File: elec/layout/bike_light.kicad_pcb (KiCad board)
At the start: 2 copper layers, 40 x 40 mm, 21 parts

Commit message: update the footprint and layout
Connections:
- net 35 renamed 32
- net 37 renamed 34
- net 42 renamed 39
- net 43 renamed 40
- net 8 renamed 7
- C2 pad 1: 14 -> 11
- C3 pad 1: 19 -> 16
- D1 pad 1: 14 -> 11
- D1 pad 2: 23 -> 20
- D2 pad 1: 15 -> 12
- D2 pad 2: 20 -> 17
- D3 pad 2: 6 -> 2
- D4 pad 2: 9 -> 2
- D5 pad 1: 11 -> 9
- D5 pad 2: 12 -> 2
- J1 pad A6: 41 -> 38
- J1 pad A8: 44 -> 41
- J1 pad B6: 41 -> 38
- J1 pad B8: 44 -> 41
- J2 pad 2: 15 -> 12
- L1 pad 2: 23 -> 20
- R1 pad 1: 18 -> 15
- R2 pad 1: 14 -> 11
- R4 pad 1: 15 -> 12
- R5 pad 1: 14 -> 11
- R5 pad 2: 21 -> 18
- R6 pad 1: 21 -> 18
- U1 pad 1: 15 -> 12
- U1 pad 2: 11 -> 9
- U1 pad 4: 11 -> 9
- U2 pad 1: 15 -> 12
- U2 pad 3: 20 -> 17
- U3 pad 10: 22 -> 19
- U3 pad 13: 14 -> 11
- U3 pad 18: 23 -> 20
- U3 pad 4: 18 -> 15
- U3 pad 6: 19 -> 16
- U3 pad 7: 20 -> 17
- U3 pad 8: 21 -> 18
- U3 pad 9: 22 -> 19
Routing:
- net 12: track 0.00 -> 62.4 mm, vias 0 -> 2
- net 15: track 62.4 -> 3.92 mm, vias 2 -> 0
- net 14: track 29.5 -> 0.00 mm, vias 2 -> 0
- net 9: track 0.00 -> 18.6 mm
- net 21: track 14.6 -> 0.00 mm, vias 2 -> 0
- net 17: track 0.00 -> 14.0 mm
- net 11: track 18.6 -> 29.5 mm, vias 0 -> 2
- net 18: track 3.92 -> 14.6 mm, vias 0 -> 2
- net 20: track 14.0 -> 5.93 mm
- net 23: track 5.93 -> 0.00 mm
- net 16: track 0.00 -> 2.25 mm
- net 19: track 2.25 -> 0.50 mm
- net 22: track 0.50 -> 0.00 mm

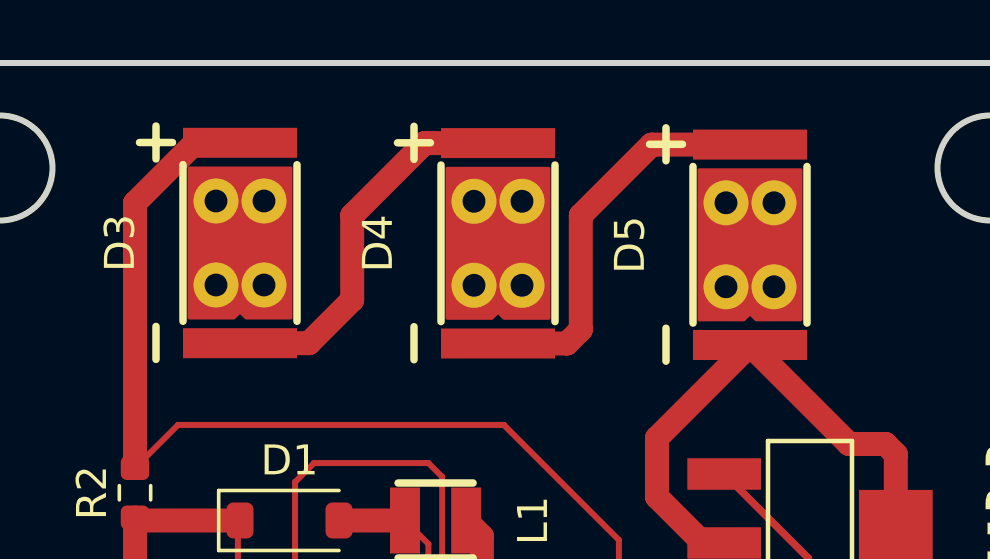
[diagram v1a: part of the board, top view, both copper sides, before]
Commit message: update footprint with thermal pad
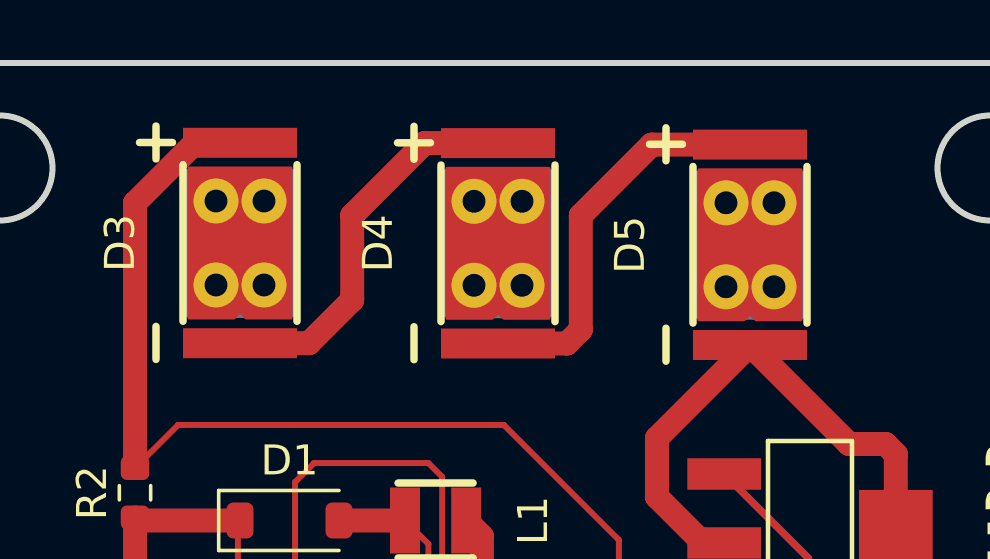
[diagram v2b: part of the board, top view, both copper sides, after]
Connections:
- net 32 renamed 35
- net 34 renamed 37
- net 39 renamed 42
- net 40 renamed 43
- net 7 renamed 8
- C2 pad 1: 11 -> 14
- C3 pad 1: 16 -> 19
- D1 pad 1: 11 -> 14
- D1 pad 2: 20 -> 23
- D2 pad 1: 12 -> 15
- D2 pad 2: 17 -> 20
- D3 pad 2: 2 -> 6
- D4 pad 2: 2 -> 9
- D5 pad 1: 9 -> 11
- D5 pad 2: 2 -> 12
- J1 pad A6: 38 -> 41
- J1 pad A8: 41 -> 44
- J1 pad B6: 38 -> 41
- J1 pad B8: 41 -> 44
- J2 pad 2: 12 -> 15
- L1 pad 2: 20 -> 23
- R1 pad 1: 15 -> 18
- R2 pad 1: 11 -> 14
- R4 pad 1: 12 -> 15
- R5 pad 1: 11 -> 14
- R5 pad 2: 18 -> 21
- R6 pad 1: 18 -> 21
- U1 pad 1: 12 -> 15
- U1 pad 2: 9 -> 11
- U1 pad 4: 9 -> 11
- U2 pad 1: 12 -> 15
- U2 pad 3: 17 -> 20
- U3 pad 10: 19 -> 22
- U3 pad 13: 11 -> 14
- U3 pad 18: 20 -> 23
- U3 pad 4: 15 -> 18
- U3 pad 6: 16 -> 19
- U3 pad 7: 17 -> 20
- U3 pad 8: 18 -> 21
- U3 pad 9: 19 -> 22
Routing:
- net 12: track 62.4 -> 0.00 mm, vias 2 -> 0
- net 15: track 3.92 -> 62.4 mm, vias 0 -> 2
- net 14: track 0.00 -> 29.5 mm, vias 0 -> 2
- net 9: track 18.6 -> 0.00 mm
- net 21: track 0.00 -> 14.6 mm, vias 0 -> 2
- net 17: track 14.0 -> 0.00 mm
- net 11: track 29.5 -> 18.6 mm, vias 2 -> 0
- net 18: track 14.6 -> 3.92 mm, vias 2 -> 0
- net 20: track 5.93 -> 14.0 mm
- net 23: track 0.00 -> 5.93 mm
- net 16: track 2.25 -> 0.00 mm
- net 19: track 0.50 -> 2.25 mm
- net 22: track 0.00 -> 0.50 mm

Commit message: layout improvements
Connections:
- U3 pad 21: (no net) -> 2
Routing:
- net 2: track 25.5 -> 10.9 mm, vias 0 -> 1
- net 14: track 29.5 -> 36.6 mm
- net 1: track 51.9 -> 47.9 mm, vias 4 -> 6
- net 5: track 39.2 -> 42.0 mm

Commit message: switch shunt resistor
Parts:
- R2: footprint Resistor_SMD:R_0603_1608Metric -> Resistor_SMD:R_1206_3216Metric
- moved R2 0.62 mm to (108.0, 113.7)
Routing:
- net 5: track 42.0 -> 40.2 mm
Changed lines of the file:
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@@
+    )
+  )
+  (footprint "Resistor_SMD:R_1206_3216Metric" (layer "F.Cu")
+    (at 108 113.7 90)
+    (descr "Resistor SMD 1206 (3216 Metric), square (rectangular) end terminal, IPC_7351 nominal, (Body size source: IPC-SM-782 page 72, https://www.pcb-3d.com/wordpress/wp-content/uploads/ipc-sm-782a_amendment_1_and_2.pdf), generated with kicad-footprint-generator")
+    (tags "resistor")
+    (attr smd)
+    (fp_text reference "R2" (at 0 -1.82 90) (layer "F.SilkS")
+        (effects (font (size 1 1) (thickness 0.15)))
+    )
+    (fp_text value "1R" (at 0 1.82 90) (layer "F.Fab")
+        (effects (font (size 1 1) (thickness 0.15)))
+    )
+    (fp_text user "${REFERENCE}" (at 0 0 90) (layer "F.Fab")
+        (effects (font (size 0.8 0.8) (thickness 0.12)))
+    )
+    (fp_line (start -0.727064 -0.91) (end 0.727064 -0.91)
+      (stroke (width 0.12) (type solid)) (layer "F.SilkS"))
+    (fp_line (start -0.727064 0.91) (end 0.727064 0.91)
+      (stroke (width 0.12) (type solid)) (layer "F.SilkS"))
+    (fp_line (start -2.28 -1.12) (end 2.28 -1.12)
+      (stroke (width 0.05) (type solid)) (layer "F.CrtYd"))
+    (fp_line (start -2.28 1.12) (end -2.28 -1.12)
+      (stroke (width 0.05) (type solid)) (layer "F.CrtYd"))
+    (fp_line (start 2.28 -1.12) (end 2.28 1.12)
+      (stroke (width 0.05) (type solid)) (layer "F.CrtYd"))
+    (fp_line (start 2.28 1.12) (end -2.28 1.12)
+      (stroke (width 0.05) (type solid)) (layer "F.CrtYd"))
+    (fp_line (start -1.6 -0.8) (end 1.6 -0.8)
+      (stroke (width 0.1) (type solid)) (layer "F.Fab"))
+    (fp_line (start -1.6 0.8) (end -1.6 -0.8)
+      (stroke (width 0.1) (type solid)) (layer "F.Fab"))
+    (fp_line (start 1.6 -0.8) (end 1.6 0.8)
+      (stroke (width 0.1) (type solid)) (layer "F.Fab"))
+    (fp_line (start 1.6 0.8) (end -1.6 0.8)
+      (stroke (width 0.1) (type solid)) (layer "F.Fab"))
+    (pad "1" smd roundrect (at -1.4625 0 90) (size 1.125 1.75) (layers "F.Cu" "F.Paste" "F.Mask") (roundrect_rratio 0.222222)
+      (net 20 "14"))
+    (pad "2" smd roundrect (at 1.4625 0 90) (size 1.125 1.75) (layers "F.Cu" "F.Paste" "F.Mask") (roundrect_rratio 0.222222)
+      (net 3 "5"))
+    (model "${KICAD6_3DMODEL_DIR}/Resistor_SMD.3dshapes/R_1206_3216Metric.wrl"
+      (offset (xyz 0 0 0))
+      (scale (xyz 1 1 1))
+      (rotate (xyz 0 0 0))
     )
   )
@@
       (net 2 "2"))
     (model "${KICAD6_3DMODEL_DIR}/Capacitor_SMD.3dshapes/C_0603_1608Metric.wrl"
-      (offset (xyz 0 0 0))
-      (scale (xyz 1 1 1))
-      (rotate (xyz 0 0 0))
-    )
-  )
-  (footprint "Resistor_SMD:R_0603_1608Metric" (layer "F.Cu")
-    (at 108 114.325 90)
-    (descr "Resistor SMD 0603 (1608 Metric), square (rectangular) end terminal, IPC_7351 nominal, (Body size source: IPC-SM-782 page 72, https://www.pcb-3d.com/wordpress/wp-content/uploads/ipc-sm-782a_amendment_1_and_2.pdf), generated with kicad-footprint-generator")
-    (tags "resistor")
-    (attr smd)
-    (fp_text reference "R2" (at 0 -1.43 90) (layer "F.SilkS")
-        (effects (font (size 1 1) (thickness 0.15)))
-    )
-    (fp_text value "1R" (at 0 1.43 90) (layer "F.Fab")
-        (effects (font (size 1 1) (thickness 0.15)))
-    )
-    (fp_text user "${REFERENCE}" (at 0 0 90) (layer "F.Fab")
-        (effects (font (size 0.4 0.4) (thickness 0.06)))
-    )
-    (fp_line (start -0.237258 -0.5225) (end 0.237258 -0.5225)
-      (stroke (width 0.12) (type solid)) (layer "F.SilkS"))
-    (fp_line (start -0.237258 0.5225) (end 0.237258 0.5225)
-      (stroke (width 0.12) (type solid)) (layer "F.SilkS"))
-    (fp_line (start -1.48 -0.73) (end 1.48 -0.73)
-      (stroke (width 0.05) (type solid)) (layer "F.CrtYd"))
-    (fp_line (start -1.48 0.73) (end -1.48 -0.73)
-      (stroke (width 0.05) (type solid)) (layer "F.CrtYd"))
-    (fp_line (start 1.48 -0.73) (end 1.48 0.73)
-      (stroke (width 0.05) (type solid)) (layer "F.CrtYd"))
-    (fp_line (start 1.48 0.73) (end -1.48 0.73)
-      (stroke (width 0.05) (type solid)) (layer "F.CrtYd"))
-    (fp_line (start -0.8 -0.4125) (end 0.8 -0.4125)
-      (stroke (width 0.1) (type solid)) (layer "F.Fab"))
-    (fp_line (start -0.8 0.4125) (end -0.8 -0.4125)
-      (stroke (width 0.1) (type solid)) (layer "F.Fab"))
-    (fp_line (start 0.8 -0.4125) (end 0.8 0.4125)
-      (stroke (width 0.1) (type solid)) (layer "F.Fab"))
-    (fp_line (start 0.8 0.4125) (end -0.8 0.4125)
-      (stroke (width 0.1) (type solid)) (layer "F.Fab"))
-    (pad "1" smd roundrect (at -0.825 0 90) (size 0.8 0.95) (layers "F.Cu" "F.Paste" "F.Mask") (roundrect_rratio 0.25)
-      (net 20 "14"))
-    (pad "2" smd roundrect (at 0.825 0 90) (size 0.8 0.95) (layers "F.Cu" "F.Paste" "F.Mask") (roundrect_rratio 0.25)
-      (net 3 "5"))
-    (model "${KICAD6_3DMODEL_DIR}/Resistor_SMD.3dshapes/R_0603_1608Metric.wrl"
       (offset (xyz 0 0 0))
       (scale (xyz 1 1 1))
@@
   (segment (start 122.65 132.5125) (end 122.95 132.5125) (width 0.2) (layer "F.Cu") (net 2))
   (via (at 118.5 117) (size 0.8) (drill 0.4) (layers "F.Cu" "B.Cu") (net 2))
-  (segment (start 108 113.5) (end 109.435 112.065) (width 0.2) (layer "F.Cu") (net 3))
   (segment (start 108 104.663604) (end 108 102.6) (width 0.8) (layer "F.Cu") (net 3))
   (segment (start 108.06 102.66) (end 111.5 102.66) (width 0.8) (layer "F.Cu") (net 3))
   (segment (start 124.13 115.9) (end 124.13 119.05) (width 0.2) (layer "F.Cu") (net 3))
-  (segment (start 108 113.5) (end 108 104.663604) (width 0.8) (layer "F.Cu") (net 3))
   (segment (start 124.13 119.05) (end 123.18 120) (width 0.2) (layer "F.Cu") (net 3))
   (segment (start 123.18 120) (end 119.9375 120) (width 0.2) (layer "F.Cu") (net 3))
+  (segment (start 108 104.663604) (end 108 112.2375) (width 0.8) (layer "F.Cu") (net 3))
   (segment (start 109.435 112.065) (end 120.295 112.065) (width 0.2) (layer "F.Cu") (net 3))
+  (segment (start 109.2625 112.2375) (end 108 112.2375) (width 0.2) (layer "F.Cu") (net 3))
   (segment (start 120.295 112.065) (end 124.13 115.9) (width 0.2) (layer "F.Cu") (net 3))
+  (segment (start 109.435 112.065) (end 109.2625 112.2375) (width 0.2) (layer "F.Cu") (net 3))
   (segment (start 110.003604 102.66) (end 111.5 102.66) (width 0.8) (layer "F.Cu") (net 3))
   (segment (start 108 102.6) (end 108.06 102.66) (width 0.4) (layer "F.Cu") (net 3))

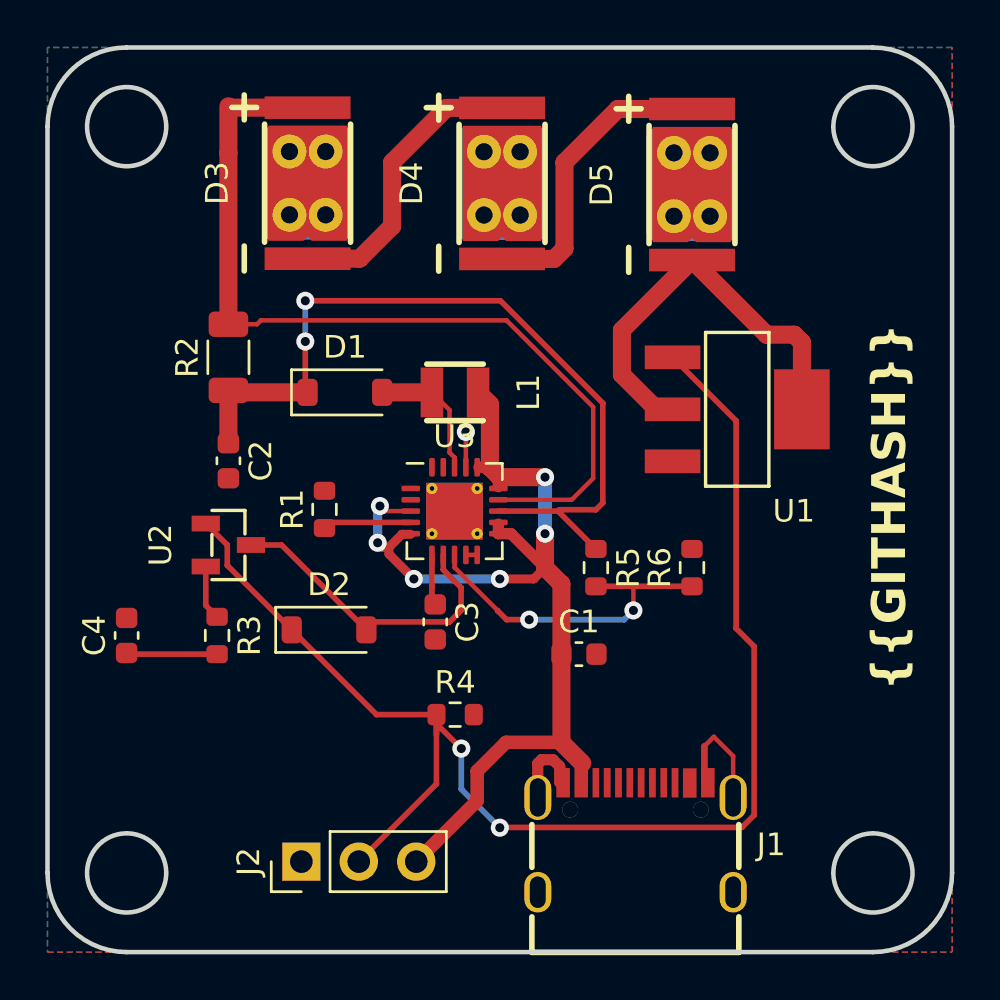
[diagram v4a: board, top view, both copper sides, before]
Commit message: improve layout and add larger inductor
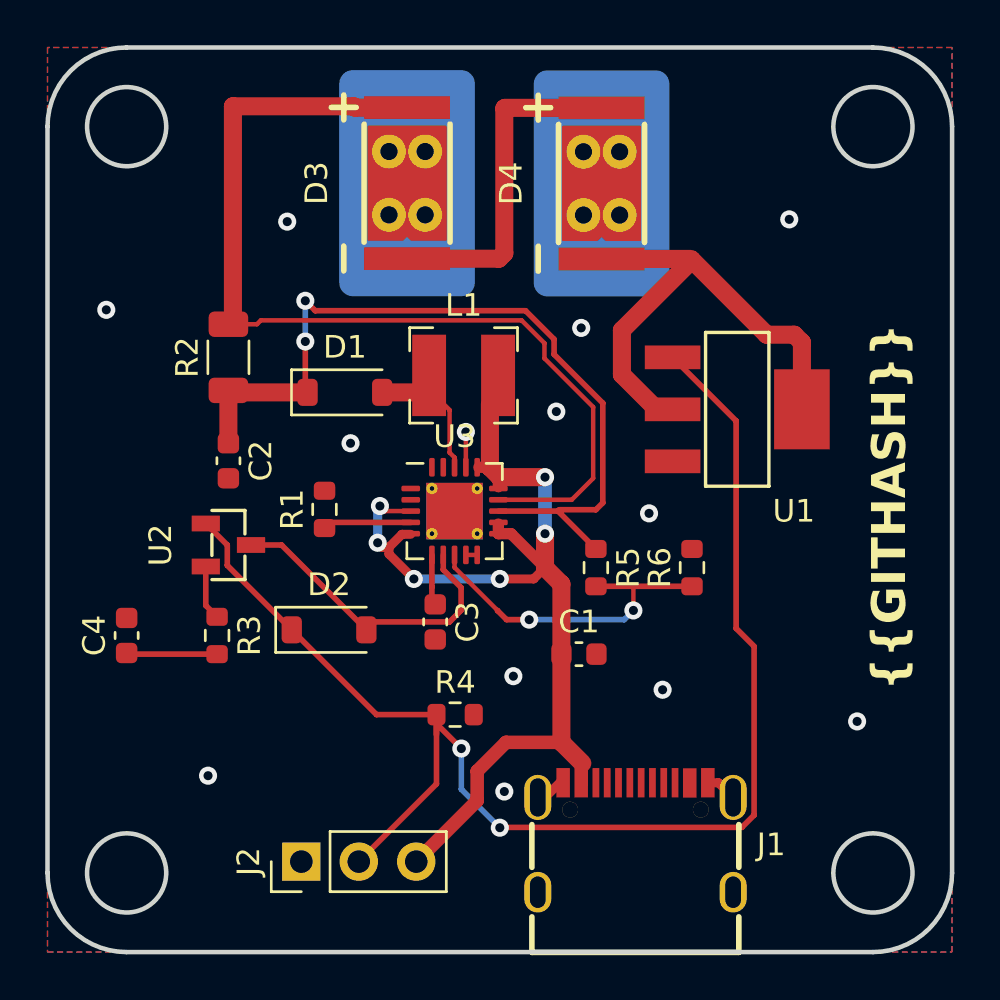
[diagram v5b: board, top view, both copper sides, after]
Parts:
- removed D5: , bike_light_lib:LED-SMD_3P-L7.0-W3.5_XL-C3570P5S10-62C3C2
- L1: value 2uH -> 2.2uH; footprint bike_light_lib:IND-SMD_L2.5-W2.0_SLW252012P -> Inductor_SMD:L_Bourns-SRN4018
- R6: value 41.2k -> 60.4k
- moved D3 4.40 mm to (115.9, 106.0)
- moved D4 4.40 mm to (124.5, 106.0)
- moved L1 0.84 mm to (118.4, 114.5)
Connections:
- net 35 renamed 32
- net 37 renamed 34
- net 42 renamed 39
- net 43 renamed 40
- C2 pad 1: 14 -> 11
- C3 pad 1: 19 -> 16
- D1 pad 1: 14 -> 11
- D1 pad 2: 23 -> 20
- D2 pad 1: 15 -> 12
- D2 pad 2: 20 -> 17
- J1 pad A6: 41 -> 38
- J1 pad A8: 44 -> 41
- J1 pad B6: 41 -> 38
- J1 pad B8: 44 -> 41
- J2 pad 2: 15 -> 12
- L1 pad 2: 23 -> 20
- R1 pad 1: 18 -> 15
- R2 pad 1: 14 -> 11
- R4 pad 1: 15 -> 12
- R5 pad 1: 14 -> 11
- R5 pad 2: 21 -> 18
- R6 pad 1: 21 -> 18
- U1 pad 1: 15 -> 12
- U1 pad 2: 11 -> 8
- U1 pad 4: 11 -> 8
- U2 pad 1: 15 -> 12
- U2 pad 3: 20 -> 17
- U3 pad 10: 22 -> 19
- U3 pad 13: 14 -> 11
- U3 pad 18: 23 -> 20
- U3 pad 4: 18 -> 15
- U3 pad 6: 19 -> 16
- U3 pad 7: 20 -> 17
- U3 pad 8: 21 -> 18
- U3 pad 9: 22 -> 19
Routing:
- net 12: track 0.00 -> 62.4 mm, vias 0 -> 2
- net 15: track 62.4 -> 3.92 mm, vias 2 -> 0
- net 14: track 36.6 -> 0.00 mm, vias 2 -> 0
- net 11: track 18.6 -> 37.0 mm, vias 0 -> 2
- net 21: track 14.9 -> 0.00 mm, vias 2 -> 0
- net 17: track 0.00 -> 14.0 mm
- net 18: track 3.92 -> 14.9 mm, vias 0 -> 2
- net 8: track 13.4 -> 22.6 mm
- net 20: track 14.0 -> 5.93 mm
- net 2: track 10.9 -> 4.73 mm, vias 1 -> 13
- net 23: track 5.93 -> 0.00 mm
- net 5: track 40.2 -> 43.4 mm
- net 16: track 0.00 -> 2.25 mm
- net 4: track 13.0 -> 15.1 mm
- net 19: track 2.25 -> 0.50 mm
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
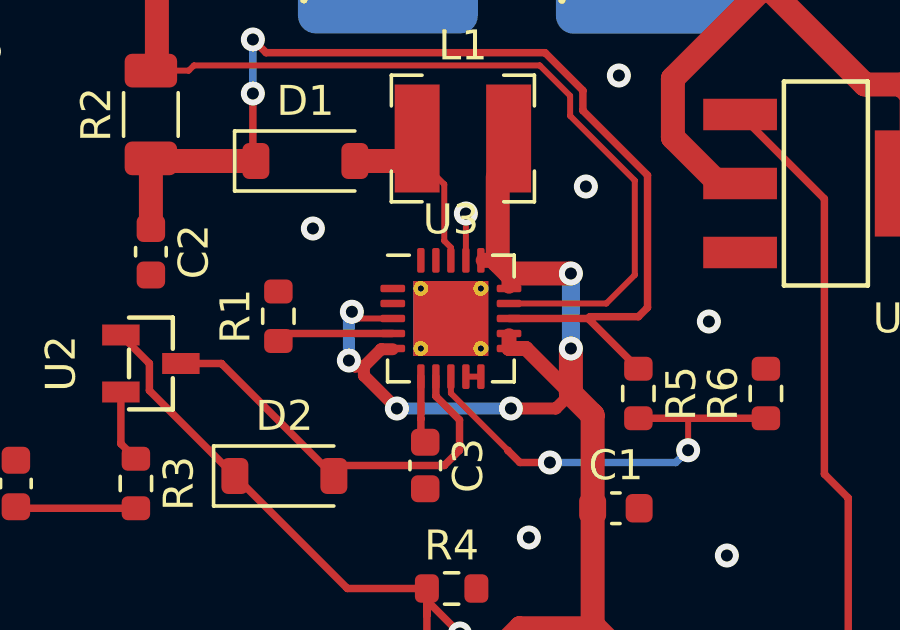
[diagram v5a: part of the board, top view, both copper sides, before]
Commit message: remove all thermal reliefs from driver chip
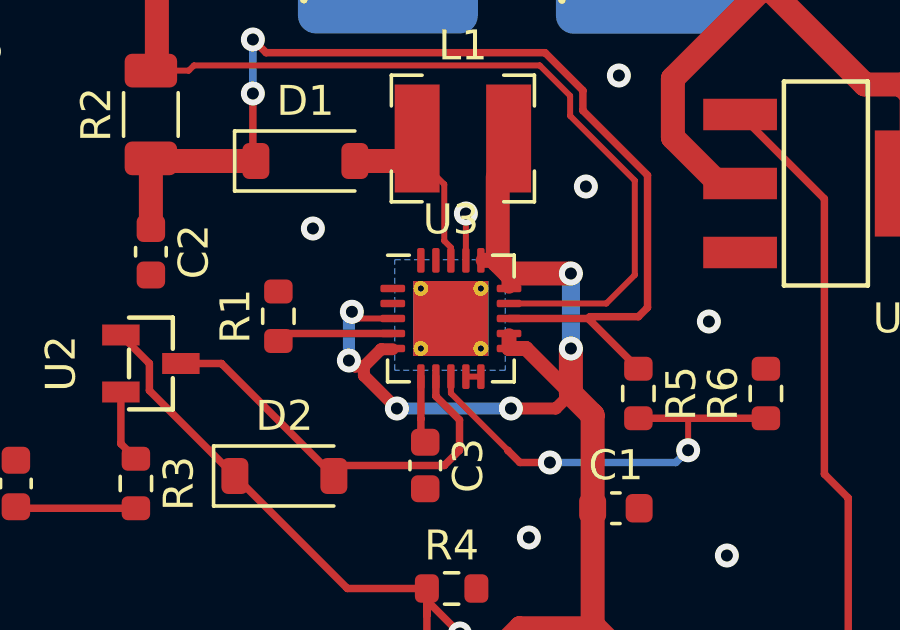
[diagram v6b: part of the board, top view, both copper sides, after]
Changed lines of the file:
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@@
+    )
+  )
+  (zone (net 2) (net_name "2") (layer "B.Cu") (hatch edge 0.5)
+    (priority 1)
+    (connect_pads yes (clearance 0.5))
+    (min_thickness 0.25) (filled_areas_thickness no)
+    (fill yes (thermal_gap 0.5) (thermal_bridge_width 0.5))
+    (polygon
+      (pts
+        (xy 116.129 118.542)
+        (xy 119.812 118.542)
+        (xy 119.812 122.225)
+        (xy 116.129 122.225)
+      )
     )
   )
